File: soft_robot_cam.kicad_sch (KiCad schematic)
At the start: 62 parts, among them J1 Conn_01x24_Socket, J2 Screw_Terminal_01x02, J3 Screw_Terminal_01x02, J4 Conn_01x05_Pin, J5 Screw_Terminal_01x02, Q1 S8050, Q2 S8050, SW1 reset, SW2 SW_DPST_x2, U1 DRV8872DDA, U2 DRV8872DDA, U3 ICM-20602, U4 AP2112K-1.2, U5 3.3v, U6 ESP32-WROVER-E, U7 TC2014-2.8VxCTTR

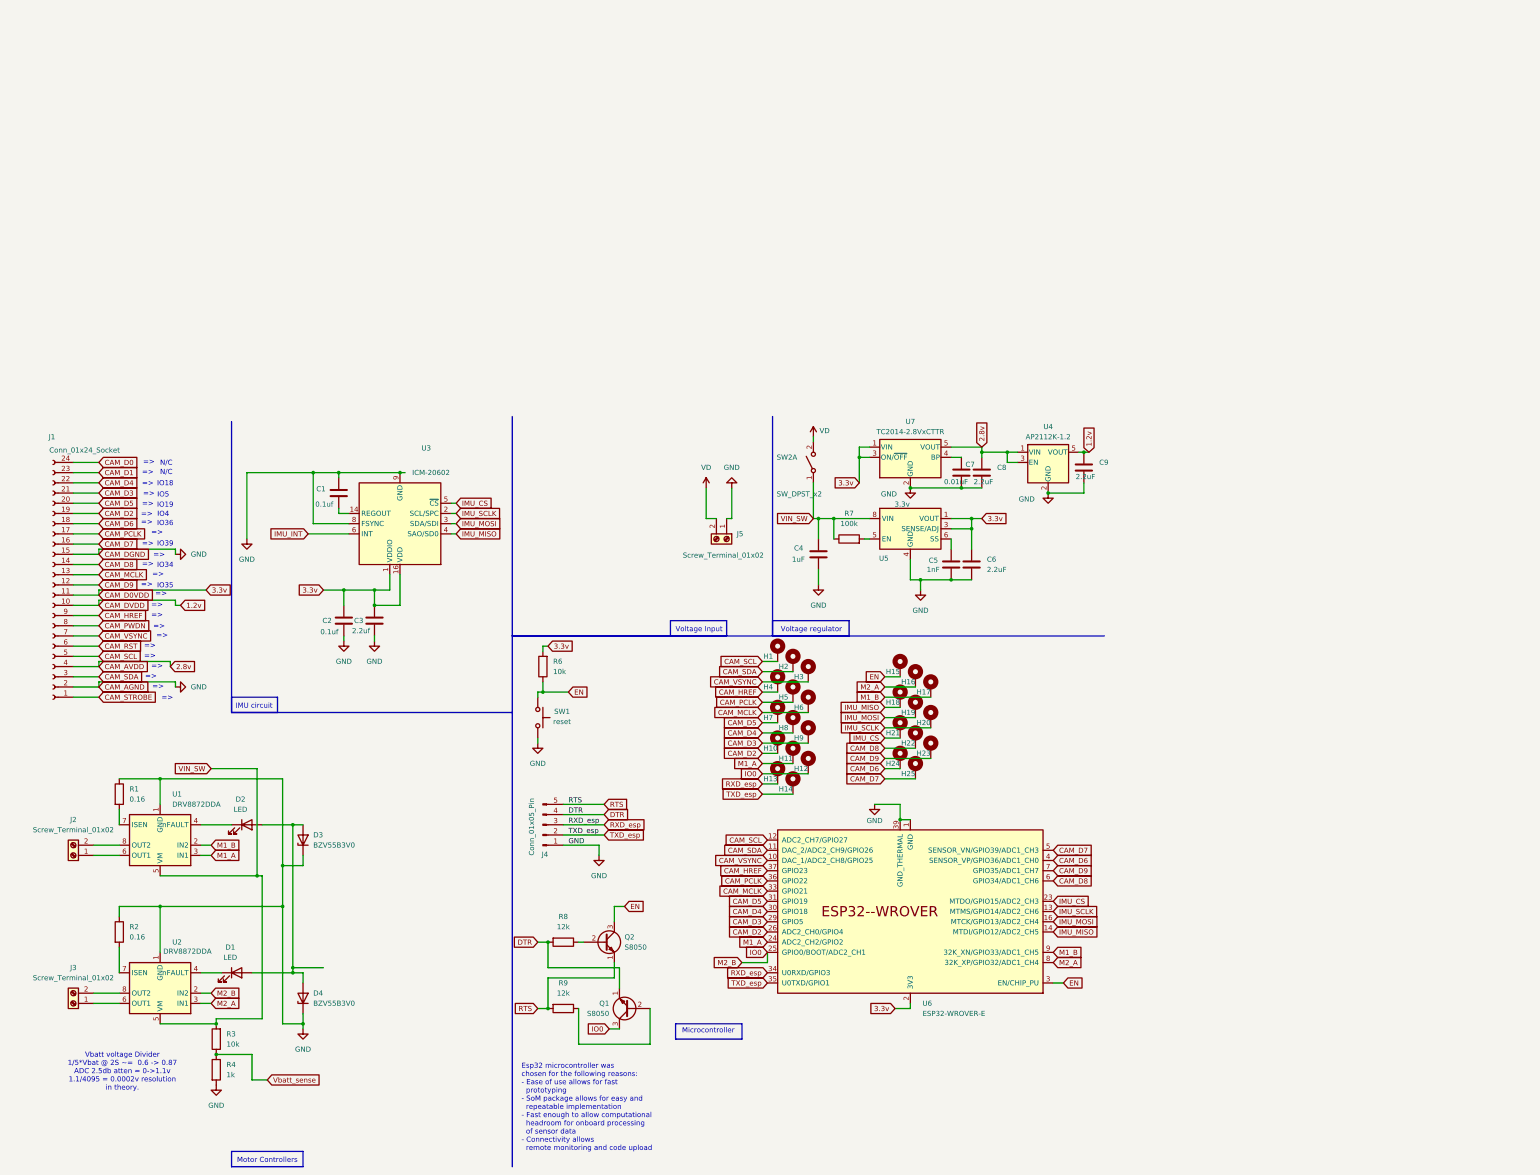
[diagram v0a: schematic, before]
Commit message: Major overhaul to layout, changed ESP to support more GPIOs, changed IMU to be standardized, changed LDOs to support the correct amperage, added buck converter for shifting LiPo voltage to 3.3V.
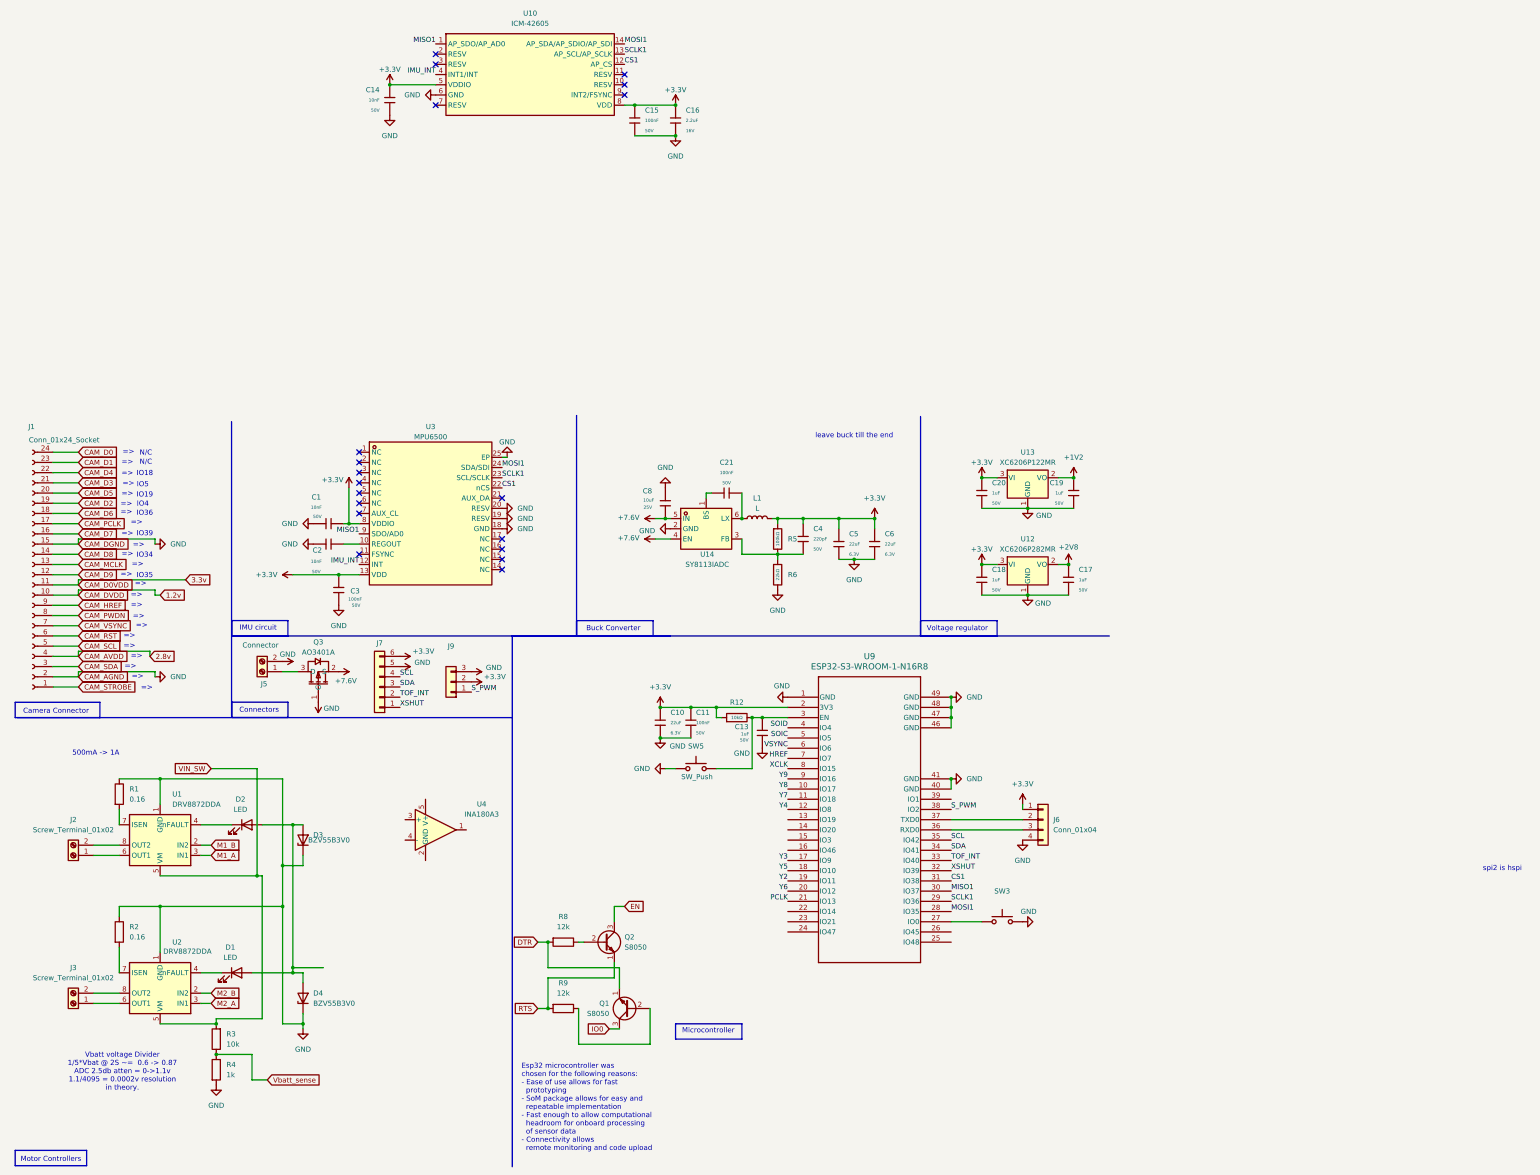
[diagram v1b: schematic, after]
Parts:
- removed C1, C2: 0.1uf, PCM_Capacitor_SMD_AKL:C_0201_0603Metric_Pad0.64x0.40mm_HandSolder, symbol Device:C
- removed C3: 2.2uf, PCM_Capacitor_SMD_AKL:C_0201_0603Metric_Pad0.64x0.40mm_HandSolder, symbol Device:C
- removed C4: 1uF, PCM_Capacitor_SMD_AKL:C_0201_0603Metric_Pad0.64x0.40mm_HandSolder, symbol Device:C
- removed C5: 1nF, PCM_Capacitor_SMD_AKL:C_0201_0603Metric_Pad0.64x0.40mm_HandSolder, symbol Device:C
- removed C6, C8, C9: 2.2uF, PCM_Capacitor_SMD_AKL:C_0201_0603Metric_Pad0.64x0.40mm_HandSolder, symbol Device:C
- removed C7: 0.01uF, PCM_Capacitor_SMD_AKL:C_0201_0603Metric_Pad0.64x0.40mm_HandSolder, symbol Device:C
- removed H1, H10, H11, H12, H13, H14, H15, H16, H17, H18, H19, H2, H20, H21, H22, H23, H24, H25, H3, H4, H5, H6, H7, H8, H9: MountingHole_Pad, TestPoint:TestPoint_Pad_D1.0mm, symbol Mechanical:MountingHole_Pad
- removed J4: Conn_01x05_Pin, Connector_PinHeader_2.54mm:PinHeader_1x05_P2.54mm_Vertical_SMD_Pin1Right, symbol Connector:Conn_01x05_Pin
- removed R6: 10k, PCM_Resistor_SMD_AKL:R_0805_2012Metric_Pad1.15x1.40mm_HandSolder, symbol Device:R
- removed R7: 100k, PCM_Resistor_SMD_AKL:R_0805_2012Metric_Pad1.15x1.40mm_HandSolder, symbol Device:R
- removed SW1: reset, Button_Switch_SMD:SW_SPST_FSMSM, symbol Switch:SW_Push
- removed SW2: SW_DPST_x2, Button_Switch_THT:SW_Slide_SPDT_Straight_CK_OS102011MS2Q, symbol Switch:SW_DPST_x2
- removed U3: ICM-20602, Package_LGA:LGA-16_3x3mm_P0.5mm_LayoutBorder3x5y, symbol Sensor_Motion:ICM-20602
- removed U4: AP2112K-1.2, Package_TO_SOT_SMD:SOT-23-5, symbol Regulator_Linear:AP2112K-1.2
- removed U5: 3.3v, Package_SO:SOIC-8-1EP_3.9x4.9mm_P1.27mm_EP2.29x3mm, symbol Regulator_Linear:ADP7142ARDZ-3.3
- removed U6: ESP32-WROVER-E, Espressif:ESP32-WROVER-E, symbol Espressif:ESP32-WROVER-E
- removed U7: TC2014-2.8VxCTTR, Package_TO_SOT_SMD:SOT-23-5, symbol Regulator_Linear:TC2014-2.8VxCTTR
- added C1, C14, C2: 10nF, PCM_JLCPCB:C_0603, symbol PCM_JLCPCB-Capacitors:0603,10nF
- added C10, C5, C6: 22uF, PCM_JLCPCB:C_0603, symbol PCM_JLCPCB-Capacitors:0603,22uF
- added C11, C15, C21, C3: 100nF, PCM_JLCPCB:C_0603, symbol PCM_JLCPCB-Capacitors:0603,100nF
- added C13, C17, C18, C19, C20: 1uF, PCM_JLCPCB:C_0603, symbol PCM_JLCPCB-Capacitors:0603,1uF
- added C16: 2.2uF, PCM_JLCPCB:C_0603, symbol PCM_JLCPCB-Capacitors:0603,2.2uF
- added C4: 220pF, PCM_JLCPCB:C_0402, symbol PCM_JLCPCB-Capacitors:0402,220pF
- added C8: 10uF, PCM_JLCPCB:C_0603, symbol PCM_JLCPCB-Capacitors:0603,10uF,(2)
- added J6: Conn_01x04, symbol Connector_Generic:Conn_01x04
- added J7: Conn_01x06, symbol Connector_Generic:Conn_01x06
- added J9: Conn_01x03, symbol Connector_Generic:Conn_01x03
- added L1: L, symbol Device:L
- added Q3: AO3401A, easyeda2kicad:SOT-23_L2.9-W1.3-P1.90-LS2.4-BR, symbol easyeda2kicad:AO3401A
- added R12: 10kΩ, PCM_JLCPCB:R_0603, symbol PCM_JLCPCB-Resistors:0603,10kΩ
- added R5: 100kΩ, PCM_JLCPCB:R_0402, symbol PCM_JLCPCB-Resistors:0402,100kΩ
- added R6: 22kΩ, PCM_JLCPCB:R_0402, symbol PCM_JLCPCB-Resistors:0402,22kΩ
- added SW3, SW5: SW_Push, symbol Switch:SW_Push
- added U10: ICM-42605, easyeda2kicad:LGA-14_L3.0-W2.5-P0.50-TL, symbol easyeda2kicad:ICM-42605
- added U12: XC6206P282MR, Package_TO_SOT_SMD:SOT-23-3, symbol Regulator_Linear:XC6206PxxxMR
- added U13: XC6206P122MR, Package_TO_SOT_SMD:SOT-23-3, symbol Regulator_Linear:XC6206PxxxMR
- added U14: SY8113IADC, easyeda2kicad:TSOT-23-6_L2.9-W1.6-P0.95-LS2.8-BL, symbol easyeda2kicad:SY8113IADC
- added U3: MPU6500, easyeda2kicad:QFN-24_L3.0-W3.0-P0.40-BL-EP, symbol easyeda2kicad:MPU6500
- added U4: INA180A3, Package_TO_SOT_SMD:SOT-23-5, symbol Amplifier_Current:INA180A3
- added U9: ESP32-S3-WROOM-1-N16R8, ESP32-S3-WROOM-1_EXP, symbol ESP32_S3_WROOM_1_N16R8:ESP32-S3-WROOM-1-N16R8
- J5: value Screw_Terminal_01x02 -> Connector
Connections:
- net VD is gone; now on net GND: J5.2 (Pin_2)
- net GND: now also C1.1, C10.2, C11.2, C13.2, C14.2, C15.2, C16.2, C17.2, C18.2, C19.2, C2.1, C20.2, C3.1, C5.2, C6.2, C8.1, J6.4 (Pin_4), J7.5 (Pin_5), J9.3 (Pin_3), Q3.1 (G), R6.2, SW3.2, SW5.1, U10.6 (GND), U12.1 (GND), U13.1 (GND), U14.2 (GND), U3.18 (GND), U3.19 (RESV), U3.20 (RESV), U3.25 (EP), U9.1 (GND), U9.40 (GND), U9.41 (GND), U9.46 (GND), U9.47 (GND), U9.48 (GND), U9.49 (GND); no longer J5.1 (Pin_1)
- net IMU_INT: now also U10.4 (INT1/INT), U3.12 (INT)
- net IO0: no longer U2.2 (IN2)
- new net: SW3.1, U9.27 (IO0)
- new net: C4.2, R5.2, R6.1, U14.3 (FB)
- new net: C13.1, R12.2, SW5.2, U9.3 (EN)
- new net: J6.3 (Pin_3), U9.36 (RXD0)
- new net: J6.2 (Pin_2), U9.37 (TXD0)
- new net: J5.1 (Pin_1), Q3.3 (D)
- new net: C21.1, U14.1 (BS)
- new net: C21.2, L1.1, U14.6 (LX)
- new net: C2.2, U3.10 (REGOUT)
- new net +1V2: C19.1, U13.2 (VO)
- new net +2V8: C17.1, U12.2 (VO)
- new net +3.3V: C1.2, C10.1, C11.1, C14.1, C15.1, C16.1, C18.1, C20.1, C3.2, C4.1, C5.1, C6.1, J6.1 (Pin_1), J7.6 (Pin_6), J9.2 (Pin_2), L1.2, R12.1, R5.1, U10.5 (VDDIO), U10.8 (VDD), U12.3 (VI), U13.3 (VI), U3.13 (VDD), U3.8 (VDDIO), U9.2 (3V3)
- new net +7.6V: C8.2, Q3.2 (S), U14.4 (EN), U14.5 (IN)
- new net CS1: U10.12 (AP_CS), U3.22 (nCS), U9.31 (IO38)
- new net HREF: U9.7 (IO7)
- new net M2_B: U2.2 (IN2)
- new net MISO1: U10.1 (AP_SDO/AP_AD0), U3.9 (SDO/AD0), U9.30 (IO37)
- new net MOSI1: U10.14 (AP_SDA/AP_SDIO/AP_SDI), U3.24 (SDA/SDI), U9.28 (IO35)
- new net PCLK: U9.21 (IO13)
- new net SCL: J7.4 (Pin_4), U9.35 (IO42)
- new net SCLK1: U10.13 (AP_SCL/AP_SCLK), U3.23 (SCL/SCLK), U9.29 (IO36)
- new net SDA: J7.3 (Pin_3), U9.34 (IO41)
- new net SOIC: U9.5 (IO5)
- new net SOID: U9.4 (IO4)
- new net S_PWM: J9.1 (Pin_1), U9.38 (IO2)
- new net TOF_INT: J7.2 (Pin_2), U9.33 (IO40)
- new net VSYNC: U9.6 (IO6)
- new net XCLK: U9.8 (IO15)
- new net XSHUT: J7.1 (Pin_1), U9.32 (IO39)
- new net Y2: U9.19 (IO11)
- new net Y3: U9.17 (IO9)
- new net Y4: U9.12 (IO8)
- new net Y5: U9.18 (IO10)
- new net Y6: U9.20 (IO12)
- new net Y7: U9.11 (IO18)
- new net Y8: U9.10 (IO17)
- new net Y9: U9.9 (IO16)
- no-connect marks 0 -> 19
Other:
- note added: "500mA -> 1A"
- note added: "Buck Converter"
- note added: "Camera Connector"
- note added: "Connectors"
- note added: "leave buck till the end"
- note added: "spi2 is hspi"
- note removed: "Voltage Input"
- moved on the sheet: J1, J5
